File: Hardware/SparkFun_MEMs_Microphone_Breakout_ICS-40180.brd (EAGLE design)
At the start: 14 x 10.2 mm, 19 parts, among them U1 OPA344, U2 ICS40180

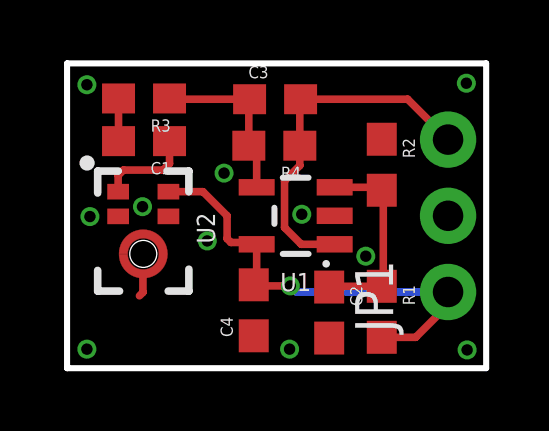
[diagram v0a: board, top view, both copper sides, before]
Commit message: changed label to fish flag output on AUD pin
added fiducials
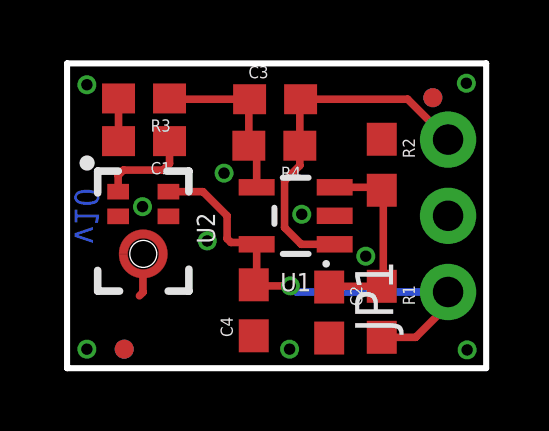
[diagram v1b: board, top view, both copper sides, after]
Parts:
- added FD1, FD2, FD3, FD4: FIDUCIALUFIDUCIAL, SparkFun-Aesthetics:FIDUCIAL-MICRO
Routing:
- net GND: vias 11 -> 10
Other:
- board text added: "v10"
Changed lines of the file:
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@@
 <setting verticaltext="up"/>
 </settings>
-<grid distance="0.05" unitdist="inch" unit="inch" style="lines" multiple="1" display="yes" altdistance="0.001" altunitdist="inch" altunit="inch"/>
+<grid distance="0.05" unitdist="inch" unit="inch" style="lines" multiple="1" display="yes" altdistance="0.005" altunitdist="inch" altunit="inch"/>
 <layers>
 <layer number="1" name="Top" color="4" fill="1" visible="yes" active="yes"/>
@@
 <layer number="47" name="Measures" color="7" fill="1" visible="no" active="yes"/>
 <layer number="48" name="Document" color="7" fill="1" visible="no" active="yes"/>
-<layer number="49" name="Reference" color="7" fill="1" visible="yes" active="yes"/>
+<layer number="49" name="Reference" color="7" fill="1" visible="no" active="yes"/>
 <layer number="50" name="dxf" color="7" fill="1" visible="no" active="yes"/>
 <layer number="51" name="tDocu" color="6" fill="1" visible="yes" active="yes"/>
@@
 <text x="1.27" y="-1.778" size="1.016" layer="27">Mic Breakout</text>
 <text x="11.43" y="-11.43" size="1.778" layer="51" font="vector" ratio="9">Pete Lewis</text>
+<text x="0.254" y="5.08" size="0.8128" layer="16" font="vector" ratio="20" rot="SMR90" align="bottom-center">v10</text>
 </plain>
 <attributes>
@@
 <element name="U$4" library="output" package="#VCC#0" value="" x="12.319" y="2.54" smashed="yes" rot="MR0"/>
 <element name="U$5" library="output" package="#AUD#0" value="" x="12.319" y="7.62" smashed="yes" rot="MR0"/>
+<element name="FD1" library="SparkFun-Aesthetics" package="FIDUCIAL-MICRO" value="FIDUCIALUFIDUCIAL" x="12.192" y="9.017" smashed="yes"/>
+<element name="FD2" library="SparkFun-Aesthetics" package="FIDUCIAL-MICRO" value="FIDUCIALUFIDUCIAL" x="12.192" y="9.017" smashed="yes" rot="MR0"/>
+<element name="FD3" library="SparkFun-Aesthetics" package="FIDUCIAL-MICRO" value="FIDUCIALUFIDUCIAL" x="1.905" y="0.635" smashed="yes"/>
+<element name="FD4" library="SparkFun-Aesthetics" package="FIDUCIAL-MICRO" value="FIDUCIALUFIDUCIAL" x="1.905" y="0.635" smashed="yes" rot="MR0"/>
 </elements>
 <signals>
@@
 <via x="7.4168" y="0.635" extent="1-16" drill="0.381"/>
 <via x="9.9568" y="3.7338" extent="1-16" drill="0.381"/>
-<via x="0.762" y="5.0546" extent="1-16" drill="0.381"/>
 <via x="2.5146" y="5.3848" extent="1-16" drill="0.381"/>
 <via x="4.6736" y="4.2418" extent="1-16" drill="0.381"/>
@@
 <mfgpreviewcolor name="substratecolor" color="0xFF786E46"/>
 </mfgpreviewcolors>
+<errors>
+</errors>
 </board>
 </drawing>

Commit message: Moved passives for tighter layout
-Moved passives to tighten up traces near + and - inputs on op amp.
-Added mic model # and flame to top silk
-Added measures
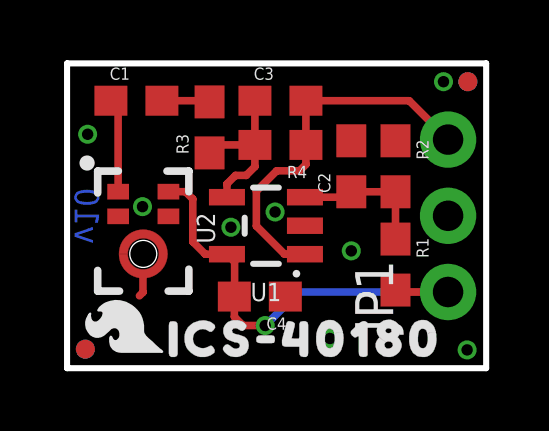
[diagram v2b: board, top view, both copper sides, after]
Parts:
- added LOGO3: SFE_LOGO_FLAME.1_INCH, SparkFun-Aesthetics:SFE_LOGO_FLAME_.1
- added U$6: (no value), output:ICS#401800
- moved C2 4.93 mm to (9.47, 6.73), turned to 90 degrees
- moved R3 2.39 mm to (4.75, 8.03), turned to 90 degrees
- moved R1 1.64 mm to (10.9, 3.45)
- moved C1 1.37 mm to (2.31, 8.92), turned to 0 degrees
- moved FD3 1.30 mm to (0.61, 0.64)
- moved FD4 1.30 mm to (0.61, 0.64)
- moved FD1 1.28 mm to (13.4, 9.55)
- moved FD2 1.28 mm to (13.4, 9.55)
- moved U1 1.04 mm to (6.63, 4.75)
- moved C4 0.50 mm to (6.43, 2.39), turned to 180 degrees
- moved R2 0.46 mm to (10.9, 6.73)
- moved R4 0.20 mm to (7.11, 7.44)
- moved C3 0.18 mm to (7.11, 8.92)
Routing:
- net N$7: track 6.62 -> 4.67 mm
- net AUD: track 11.9 -> 12.6 mm
- net GND: vias 10 -> 8
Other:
- board text added: "Units: INCHES"

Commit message: Changed values to extend freq response
-Changes passives to extend frequency rolloffs on the opamp circuit. It's not 7.2Hz-19.7KHz, which better matches the capabilities of the new mic.
-Added SparkFun "name" logo to schematic - note, I copied vectors from library so it isn't a proper symbol/device.
-rearranged schematic and labeled "mic" and "gainstage" sections
-Capitalized the S in MEMS on the bottom silk.
-Made measures text size all the same at 0.05inch
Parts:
- C3: value 100pF -> 27pF
- R3: value 1.5k -> 4.7k
- R4: value 100k -> 300k
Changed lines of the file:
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@@
 <drawing>
 <settings>
-<setting alwaysvectorfont="yes"/>
+<setting alwaysvectorfont="no"/>
 <setting keepoldvectorfont="yes"/>
 <setting verticaltext="up"/>
 </settings>
-<grid distance="0.05" unitdist="inch" unit="inch" style="lines" multiple="1" display="yes" altdistance="0.001" altunitdist="inch" altunit="inch"/>
+<grid distance="0.05" unitdist="inch" unit="inch" style="lines" multiple="1" display="yes" altdistance="0.005" altunitdist="inch" altunit="inch"/>
 <layers>
 <layer number="1" name="Top" color="4" fill="1" visible="yes" active="yes"/>
@@
 <layer number="37" name="tTest" color="7" fill="1" visible="no" active="yes"/>
 <layer number="38" name="bTest" color="7" fill="1" visible="no" active="yes"/>
-<layer number="39" name="tKeepout" color="4" fill="11" visible="yes" active="yes"/>
+<layer number="39" name="tKeepout" color="4" fill="11" visible="no" active="yes"/>
 <layer number="40" name="bKeepout" color="1" fill="11" visible="no" active="yes"/>
 <layer number="41" name="tRestrict" color="4" fill="10" visible="no" active="yes"/>
@@
 <text x="11.43" y="-11.43" size="1.778" layer="51" font="vector" ratio="9">Pete Lewis</text>
 <text x="0.254" y="5.08" size="0.8128" layer="16" font="vector" ratio="20" rot="SMR90" align="bottom-center">v10</text>
-<dimension x1="0" y1="10.16" x2="0" y2="0" x3="-7.62" y3="5.08" textsize="1.778" textratio="15" layer="47" width="0.0762" unit="inch" precision="3"/>
-<dimension x1="13.97" y1="10.16" x2="0" y2="10.16" x3="6.985" y3="17.78" textsize="1.778" textratio="15" layer="47" width="0.0762" unit="inch" precision="3"/>
-<dimension x1="13.97" y1="0" x2="12.7" y2="2.54" x3="25.4" y3="1.27" textsize="1.778" textratio="15" layer="47" dtype="vertical" width="0.0762" unit="inch" precision="3"/>
-<dimension x1="13.97" y1="0" x2="12.7" y2="5.08" x3="21.59" y3="2.54" textsize="1.778" textratio="15" layer="47" dtype="vertical" width="0.0762" unit="inch" precision="3"/>
-<dimension x1="13.97" y1="0" x2="12.7" y2="7.62" x3="17.78" y3="3.81" textsize="1.778" textratio="15" layer="47" dtype="vertical" width="0.0762" unit="inch" precision="3"/>
-<dimension x1="0" y1="0" x2="2.54" y2="3.81" x3="1.27" y3="13.97" textsize="1.778" textratio="15" layer="47" dtype="horizontal" width="0.0762" unit="inch" precision="3"/>
+<dimension x1="0" y1="10.16" x2="0" y2="0" x3="-7.62" y3="5.08" textsize="1.27" textratio="15" layer="47" width="0.0762" unit="inch" precision="3"/>
+<dimension x1="13.97" y1="10.16" x2="0" y2="10.16" x3="6.985" y3="17.78" textsize="1.27" textratio="15" layer="47" width="0.0762" unit="inch" precision="3"/>
+<dimension x1="13.97" y1="0" x2="12.7" y2="2.54" x3="21.59" y3="1.27" textsize="1.27" textratio="15" layer="47" dtype="vertical" width="0.0762" unit="inch" precision="3"/>
+<dimension x1="13.97" y1="0" x2="12.7" y2="5.08" x3="17.78" y3="2.54" textsize="1.27" textratio="15" layer="47" dtype="vertical" width="0.0762" unit="inch" precision="3"/>
+<dimension x1="13.97" y1="0" x2="12.7" y2="7.62" x3="25.4" y3="3.81" textsize="1.27" textratio="15" layer="47" dtype="vertical" width="0.0762" unit="inch" precision="3"/>
+<dimension x1="0" y1="0" x2="2.54" y2="3.81" x3="1.27" y3="13.97" textsize="1.27" textratio="15" layer="47" dtype="horizontal" width="0.0762" unit="inch" precision="3"/>
 <dimension x1="0" y1="0" x2="2.54" y2="3.81" x3="-3.81" y3="1.905" textsize="1.27" textratio="15" layer="47" dtype="vertical" width="0.0762" unit="inch"/>
-<text x="-2.54" y="22.86" size="1.778" layer="47" font="vector">Units: INCHES</text>
+<text x="-2.54" y="22.86" size="1.27" layer="47" font="vector">Units: INCHES</text>
 </plain>
 <attributes>
@@
 <attribute name="VALUE" value="10k" x="10.8204" y="5.5245" size="0.4064" layer="27" rot="R270"/>
 </element>
-<element name="R3" library="SparkFun-Resistors" package="0603" value="1.5k" x="4.7498" y="8.0264" smashed="yes" rot="R90">
+<element name="R3" library="SparkFun-Resistors" package="0603" value="4.7k" x="4.7498" y="8.0264" smashed="yes" rot="R90">
 <attribute name="NAME" x="4.0513" y="7.1374" size="0.4064" layer="25" rot="R90"/>
-<attribute name="PROD_ID" value="RES-08306" x="4.7498" y="8.0264" size="1.778" layer="27" rot="R90" display="off"/>
-<attribute name="VALUE" value="1.5k" x="5.3848" y="9.1059" size="0.4064" layer="27" rot="R90"/>
-</element>
-<element name="R4" library="SparkFun-Resistors" package="0603" value="100k" x="7.112" y="7.4422" smashed="yes" rot="R180">
+<attribute name="PROD_ID" value="RES-07857" x="4.7498" y="8.0264" size="1.778" layer="27" rot="R90" display="off"/>
+<attribute name="VALUE" value="4.7k" x="5.3848" y="9.1059" size="0.4064" layer="27" rot="R90"/>
+</element>
+<element name="R4" library="SparkFun-Resistors" package="0603" value="300k" x="7.112" y="7.4422" smashed="yes" rot="R180">
 <attribute name="NAME" x="8.001" y="6.7437" size="0.4064" layer="25" rot="R180"/>
-<attribute name="PROD_ID" value="RES-07828" x="7.112" y="7.4422" size="1.778" layer="27" rot="R180" display="off"/>
-<attribute name="VALUE" value="100k" x="8.3185" y="7.5692" size="0.4064" layer="27"/>
-</element>
-<element name="C3" library="SparkFun-Capacitors" package="0603" value="100pF" x="7.112" y="8.9154" smashed="yes">
+<attribute name="PROD_ID" value="RES-10809" x="7.112" y="7.4422" size="1.778" layer="27" rot="R180" display="off"/>
+<attribute name="VALUE" value="300k" x="8.3185" y="7.5692" size="0.4064" layer="27"/>
+</element>
+<element name="C3" library="SparkFun-Capacitors" package="0603" value="27pF" x="7.112" y="8.9154" smashed="yes">
 <attribute name="NAME" x="6.223" y="9.6139" size="0.4064" layer="25"/>
-<attribute name="PROD_ID" value="CAP-07883" x="7.112" y="8.9154" size="1.778" layer="27" display="off"/>
-<attribute name="VALUE" value="100pF" x="8.3185" y="8.7884" size="0.4064" layer="27"/>
+<attribute name="PROD_ID" value="CAP-09989" x="7.112" y="8.9154" size="1.778" layer="27" display="off"/>
+<attribute name="VALUE" value="27pF" x="8.3185" y="8.7884" size="0.4064" layer="27"/>
 </element>
 <element name="C4" library="SparkFun-Capacitors" package="0603" value="0.1uF" x="6.4262" y="2.3876" smashed="yes" rot="R180">
